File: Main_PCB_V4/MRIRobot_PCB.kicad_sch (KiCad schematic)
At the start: 339 parts, among them J1 Conn_01x05, J10 Homing, J11 Homing, J12 Homing, J13 Homing, J14 Homing, J15 Homing, J16 Homing, J17 Conn_01x08, J18 Conn_01x08, J19 Conn_01x08, J2 Conn_01x05, J20 Conn_01x08, J21 Conn_01x08, J22 Conn_01x03, J23 Conn_01x03, J24 Conn_01x08, J25 Conn_01x03, J26 Conn_01x03, J27 Conn_01x08, J28 RJCSE538001, J3 Conn_01x05, J32 RJCSE538001, J33 RJCSE538001, J34 RJCSE538001, J4 USB_C_Receptacle_USB2.0_16P, J5 Conn_01x05, J6 Conn_01x05, J7 Conn_01x05, J8 Conn_01x05, J9 Power In, Q1 SUD08P06-155L, SW1 5V Enable, SW2 3.3V Enable, SW3 Toggle_Switch0, SW4 Toggle_Switch1, SW5 Toggle_Switch2, SW6 Toggle_Switch3, U1 NUCLEO-F446RE, U2 FT231XS, U3 CMOD_A7_FPGA, U4 LM22676MR-5, U5 LM22676MR-ADJ, U6 LSF0108, U7 LSF0108, U8 LSF0108

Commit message: started hierarchy for USBC block in schematic
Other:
- added sheet USBC Connector (USBC-Power.kicad_sch)
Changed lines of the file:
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@@
 		)
+	)
+	(sheet
+		(at 499.11 325.12)
+		(size 44.45 33.02)
+		(exclude_from_sim no)
+		(in_bom yes)
+		(on_board yes)
+		(dnp no)
+		(fields_autoplaced yes)
+		(stroke
+			(width 0.1524)
+			(type solid)
+		)
+		(fill
+			(color 0 0 0 0.0000)
+		)
+		(property "Sheetname" "USBC Connector"
+			(at 499.11 324.4084 0)
+			(show_name yes)
+			(effects
+				(font
+					(size 1.27 1.27)
+				)
+				(justify left bottom)
+			)
+		)
+		(property "Sheetfile" "USBC-Power.kicad_sch"
+			(at 499.11 358.7246 0)
+			(show_name yes)
+			(effects
+				(font
+					(size 1.27 1.27)
+				)
+				(justify left top)
+			)
+		)
+		(pin "UART_RX" output
+			(at 499.11 331.47 180)
+			(effects
+				(font
+					(size 1.27 1.27)
+				)
+				(justify left)
+			)
+		)
+		(pin "USBC_3.3V" input
+			(at 499.11 339.09 180)
+			(effects
+				(font
+					(size 1.27 1.27)
+				)
+				(justify left)
+			)
+		)
+		(pin "UART_TX" input
+			(at 499.11 335.28 180)
+			(effects
+				(font
+					(size 1.27 1.27)
+				)
+				(justify left)
+			)
+		)
+		(pin "USBC_5V" output
+			(at 499.11 345.44 180)
+			(effects
+				(font
+					(size 1.27 1.27)
+				)
+				(justify left)
+			)
+		)
+		(pin "USBC_GND" input
+			(at 499.11 350.52 180)
+			(effects
+				(font
+					(size 1.27 1.27)
+				)
+				(justify left)
+			)
+		)
+		(instances)
 	)
 	(sheet_instances

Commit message: Added hierarchy for encoders. Started hierarchy for power.
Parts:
- removed C1: 0.1u, Capacitor_SMD:C_0603_1608Metric_Pad1.08x0.95mm_HandSolder, symbol Device:C
- removed C17, C18, C19: 0.1uF, Capacitor_SMD:C_0805_2012Metric_Pad1.18x1.45mm_HandSolder, symbol Device:C
- removed C20, C21, C22, C23, C24, C25, C26, C27, C28, C29, C30, C31, C32, C33, C34, C35, C36, C37, C38, C39, C40: 100 pF, Capacitor_SMD:C_0805_2012Metric_Pad1.18x1.45mm_HandSolder, symbol Device:C
- removed D1: D, Diode_SMD:D_SMA_Handsoldering, symbol Device:D
- removed D100, D101, D102, D103, D104, D105, D106, D107, D108, D110, D17, D19, D20, D21, D22, D23, D24, D25, D26, D27, D28, D29, D30, D31, D32, D33, D34, D35, D36, D37, D38, D86, D88, D89, D90, D91, D92, D93, D94, D95, D96, D97, D98, D99: D_TVS, Diode_SMD:D_SOD-123F, symbol Device:D_TVS
- removed D111, D87: D, Diode_SMD:D_SOD-128, symbol Device:D
- removed D13, D14: LED, LED_SMD:LED_0805_2012Metric_Pad1.15x1.40mm_HandSolder, symbol Device:LED
- removed J1, J2, J3, J5, J6, J7, J8: Conn_01x05, Connector_JST:JST_EH_B5B-EH-A_1x05_P2.50mm_Vertical, symbol Connector_Generic:Conn_01x05
- removed J28, J32, J33, J34: RJCSE538001, RJCSE538001:AMPHENOL_RJCSE538001, symbol RJCSE538001:RJCSE538001
- removed J4: USB_C_Receptacle_USB2.0_16P, Connector_USB:USB_C_Receptacle_GCT_USB4105-xx-A_16P_TopMnt_Horizontal, symbol Connector:USB_C_Receptacle_USB2.0_16P
- removed R1, R2, R3: 200k, Capacitor_SMD:C_0805_2012Metric_Pad1.18x1.45mm_HandSolder, symbol Device:R
- removed R10, R11, R12, R15, R16, R17, R18, R19, R20, R23, R24, R25, R26, R27, R28, R29, R30, R31, R7, R8, R9: 1k, Capacitor_SMD:C_0805_2012Metric_Pad1.18x1.45mm_HandSolder, symbol Device:R
- removed R110, R111, R112, R113, R114, R115, R116, R117, R118, R119, R120, R121, R122, R123, R124, R125, R126, R127, R128, R129, R130: 10k, Capacitor_SMD:C_0805_2012Metric_Pad1.18x1.45mm_HandSolder, symbol Device:R
- removed R13, R14: 5.1k, Resistor_SMD:R_0603_1608Metric_Pad0.98x0.95mm_HandSolder, symbol Device:R
- removed R21, R22: 27, Resistor_SMD:R_0603_1608Metric_Pad0.98x0.95mm_HandSolder, symbol Device:R
- removed R4, R5: 290, Capacitor_SMD:C_0805_2012Metric_Pad1.18x1.45mm_HandSolder, symbol Device:R
- removed U2: FT231XS, Package_SO:SSOP-20_3.9x8.7mm_P0.635mm, symbol Interface_USB:FT231XS
- removed U3: CMOD_A7_FPGA, CMOD_FPGA:CMODA7, symbol CMOD_FPGA:CMOD_A7
- removed U6, U7, U8: LSF0108, Package_SO:TSSOP-20_4.4x6.5mm_P0.65mm, symbol level_shifters:LSF0108
- U1: footprint NUCLEO-F446RE:MODULE_NUCLEO-F446RE -> nucleo446-footprint:MODULE_NUCLEO-F446RE
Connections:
- net GND: no longer U1.CN6_6 (CN6_GND)
- no-connect marks 68 -> 47
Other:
- added sheet EncoderBlock (EncoderBlock.kicad_sch)
- note added: "Note 3V3 CN7_18 is wired directly to CN6_5. Also +5V CN7_16 is wired diretly to CN6_4. These are supplied by VR U4."
- note removed: "CMOD7 FPGA"
- note removed: "Encoder pulldown"
- note removed: "Encoders"
- note removed: "Ethernet Encoder Wires"
- note removed: "USBC Connector"

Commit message: moved all power sources to own sheet
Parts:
- removed C10, C11: 120uF, Capacitor_THT:CP_Radial_D6.3mm_P2.50mm, symbol Device:C
- removed C2, C3: 22uF, Capacitor_THT:CP_Radial_D5.0mm_P2.00mm, symbol Device:C
- removed C4, C5: 6.8uF, Capacitor_SMD:C_0805_2012Metric, symbol Device:C
- removed C8, C9: 10nF, Capacitor_SMD:C_0805_2012Metric, symbol Device:C
- removed D2, D3, D4, D5: D, Diode_SMD:D_SMA_Handsoldering, symbol Device:D
- removed L1, L2: 8.2uH, Inductor_SMD:L_7.3x7.3_H3.5, symbol Device:L
- removed R56, R58: 6.2k, Resistor_SMD:R_0805_2012Metric, symbol Device:R
- removed R57, R59: 1k, Resistor_SMD:R_0805_2012Metric, symbol Device:R
- removed R62: 976, Resistor_SMD:R_0805_2012Metric, symbol Device:R
- removed R63: 1.54k, Resistor_SMD:R_0805_2012Metric, symbol Device:R
- removed SW1: 5V Enable, Button_Switch_THT:SW_Slide_SPDT_Straight_CK_OS102011MS2Q, symbol Switch:SW_SPDT
- removed SW2: 3.3V Enable, Button_Switch_THT:SW_Slide_SPDT_Straight_CK_OS102011MS2Q, symbol Switch:SW_SPDT
- removed U4: LM22676MR-5, Package_SO:TI_SO-PowerPAD-8, symbol Regulator_Switching:LM22676MR-5
- removed U5: LM22676MR-ADJ, Package_SO:TI_SO-PowerPAD-8, symbol Regulator_Switching:LM22676MR-ADJ
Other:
- note added: "See sheet for details on 3 possible power sources"
- note removed: "Voltage Converters"

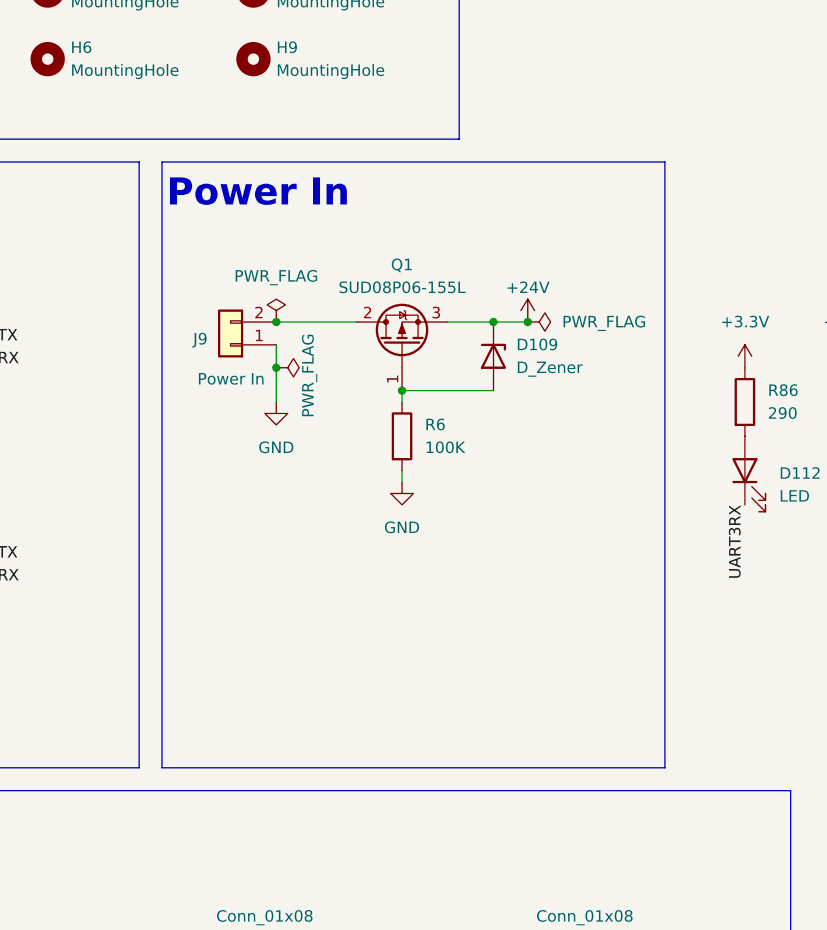
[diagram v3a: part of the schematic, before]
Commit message: added J9 connector and 5V 3.3V buck converters to schematic
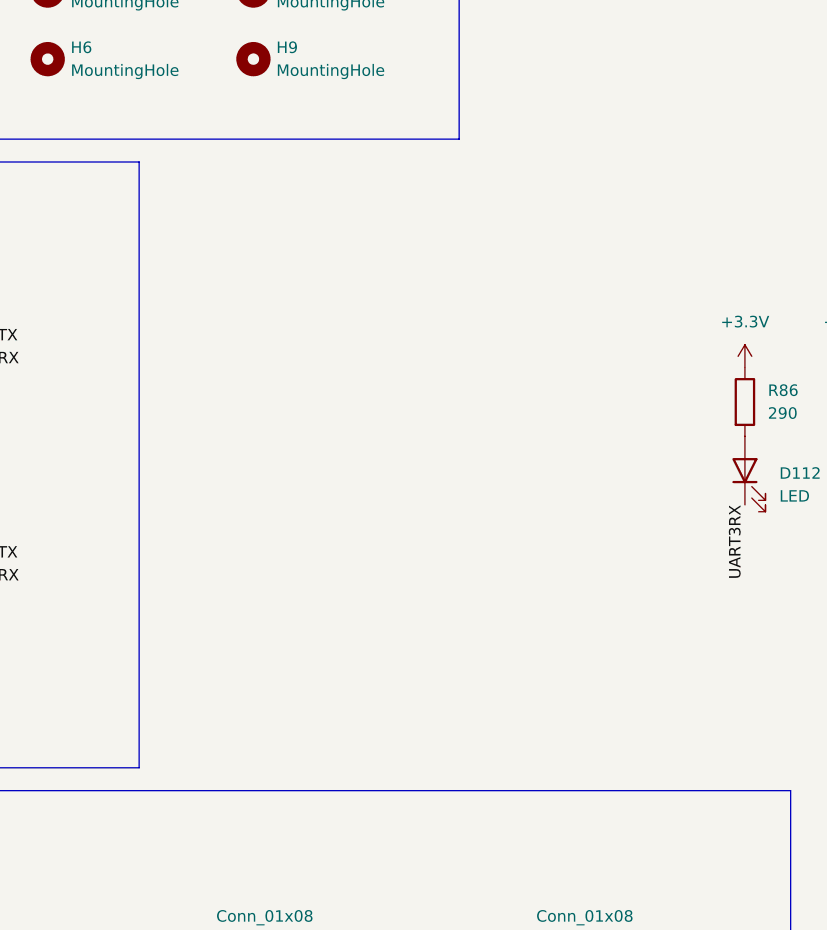
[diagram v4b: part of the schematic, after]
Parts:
- removed D109: D_Zener, Diode_SMD:D_SMA_Handsoldering, symbol Device:D_Zener
- removed J9: Power In, Connector_AMASS:AMASS_XT60-M_1x02_P7.20mm_Vertical, symbol Connector_Generic:Conn_01x02
- removed Q1: SUD08P06-155L, Package_TO_SOT_SMD:TO-252-2, symbol Transistor_FET:SUD08P06-155L
- removed R6: 100K, Resistor_SMD:R_0805_2012Metric, symbol Device:R
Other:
- note removed: "Power In"
